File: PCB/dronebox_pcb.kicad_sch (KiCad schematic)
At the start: 17 parts, among them J101 Conn_02x05_Odd_Even, J102 Barrel_Jack_Switch, J103 Conn_01x02_Female, J104 Conn_01x02_Female, U101 LM386

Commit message: assign fps
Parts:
- C101, C102: footprint (none) -> Capacitor_THT:CP_Radial_D6.3mm_P2.50mm
- C103: footprint (none) -> Capacitor_THT:C_Disc_D4.7mm_W2.5mm_P5.00mm
- J101: footprint (none) -> Connector_IDC:IDC-Header_2x05_P2.54mm_Vertical
- J102: footprint (none) -> Connector_BarrelJack:BarrelJack_GCT_DCJ200-10-A_Horizontal
- J103, J104: footprint (none) -> Connector_PinHeader_2.54mm:PinHeader_1x02_P2.54mm_Vertical
- R101, R102, R103, R104, R105: footprint (none) -> Resistor_THT:R_Axial_DIN0207_L6.3mm_D2.5mm_P2.54mm_Vertical
- U101: footprint (none) -> Package_DIP:DIP-8_W7.62mm_Socket_LongPads
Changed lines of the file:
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@@
       (effects (font (size 1.27 1.27)) (justify left))
     )
-    (property "Footprint" "" (id 2) (at 87.122 170.18 90)
+    (property "Footprint" "Resistor_THT:R_Axial_DIN0207_L6.3mm_D2.5mm_P2.54mm_Vertical" (id 2) (at 87.122 170.18 90)
       (effects (font (size 1.27 1.27)) hide)
     )
@@
     (property "Reference" "R102" (id 0) (at 109.22 170.18 90))
     (property "Value" "10K" (id 1) (at 109.22 172.72 90))
-    (property "Footprint" "" (id 2) (at 109.22 178.308 90)
+    (property "Footprint" "Resistor_THT:R_Axial_DIN0207_L6.3mm_D2.5mm_P2.54mm_Vertical" (id 2) (at 109.22 178.308 90)
       (effects (font (size 1.27 1.27)) hide)
     )
@@
     (property "Reference" "R103" (id 0) (at 185.42 168.91 90))
     (property "Value" "10M" (id 1) (at 185.42 171.45 90))
-    (property "Footprint" "" (id 2) (at 185.42 177.038 90)
+    (property "Footprint" "Resistor_THT:R_Axial_DIN0207_L6.3mm_D2.5mm_P2.54mm_Vertical" (id 2) (at 185.42 177.038 90)
       (effects (font (size 1.27 1.27)) hide)
     )
@@
     (property "Reference" "R104" (id 0) (at 186.69 158.75 90))
     (property "Value" "680K" (id 1) (at 186.69 161.29 90))
-    (property "Footprint" "" (id 2) (at 186.69 166.878 90)
+    (property "Footprint" "Resistor_THT:R_Axial_DIN0207_L6.3mm_D2.5mm_P2.54mm_Vertical" (id 2) (at 186.69 166.878 90)
       (effects (font (size 1.27 1.27)) hide)
     )
@@
     (property "Reference" "R105" (id 0) (at 210.82 158.75 90))
     (property "Value" "100K" (id 1) (at 210.82 161.29 90))
-    (property "Footprint" "" (id 2) (at 210.82 166.878 90)
+    (property "Footprint" "Resistor_THT:R_Axial_DIN0207_L6.3mm_D2.5mm_P2.54mm_Vertical" (id 2) (at 210.82 166.878 90)
       (effects (font (size 1.27 1.27)) hide)
     )
@@
       (effects (font (size 1.27 1.27)) (justify left))
     )
-    (property "Footprint" "" (id 2) (at 124.46 184.15 0)
+    (property "Footprint" "Connector_PinHeader_2.54mm:PinHeader_1x02_P2.54mm_Vertical" (id 2) (at 124.46 184.15 0)
       (effects (font (size 1.27 1.27)) hide)
     )
@@
     (property "Reference" "J104" (id 0) (at 159.9057 167.64 0))
     (property "Value" "Conn_01x02_Female" (id 1) (at 157.3657 172.72 0))
-    (property "Footprint" "" (id 2) (at 163.83 168.91 0)
+    (property "Footprint" "Connector_PinHeader_2.54mm:PinHeader_1x02_P2.54mm_Vertical" (id 2) (at 163.83 168.91 0)
       (effects (font (size 1.27 1.27)) hide)
     )
@@
       (effects (font (size 1.27 1.27)) (justify left))
     )
-    (property "Footprint" "" (id 2) (at 101.2952 191.77 0)
+    (property "Footprint" "Capacitor_THT:CP_Radial_D6.3mm_P2.50mm" (id 2) (at 101.2952 191.77 0)
       (effects (font (size 1.27 1.27)) hide)
     )
@@
       (effects (font (size 1.27 1.27)) (justify left))
     )
-    (property "Footprint" "" (id 2) (at 120.3452 184.15 0)
+    (property "Footprint" "Capacitor_THT:CP_Radial_D6.3mm_P2.50mm" (id 2) (at 120.3452 184.15 0)
       (effects (font (size 1.27 1.27)) hide)
     )
@@
     (property "Reference" "C103" (id 0) (at 138.43 168.91 90))
     (property "Value" "C" (id 1) (at 138.43 171.45 90))
-    (property "Footprint" "" (id 2) (at 142.24 175.5648 0)
+    (property "Footprint" "Capacitor_THT:C_Disc_D4.7mm_W2.5mm_P5.00mm" (id 2) (at 142.24 175.5648 0)
       (effects (font (size 1.27 1.27)) hide)
     )
@@
     (property "Reference" "J102" (id 0) (at 40.5765 184.15 0))
     (property "Value" "Barrel_Jack_Switch" (id 1) (at 40.5765 186.69 0))
-    (property "Footprint" "" (id 2) (at 40.64 194.056 0)
+    (property "Footprint" "Connector_BarrelJack:BarrelJack_GCT_DCJ200-10-A_Horizontal" (id 2) (at 40.64 194.056 0)
       (effects (font (size 1.27 1.27)) hide)
     )
@@
     (property "Reference" "J101" (id 0) (at 40.64 165.1 0))
     (property "Value" "Conn_02x05_Odd_Even" (id 1) (at 40.64 167.64 0))
-    (property "Footprint" "" (id 2) (at 39.37 176.53 0)
+    (property "Footprint" "Connector_IDC:IDC-Header_2x05_P2.54mm_Vertical" (id 2) (at 39.37 176.53 0)
       (effects (font (size 1.27 1.27)) hide)
     )
@@
       (effects (font (size 1.27 1.27)) (justify left))
     )
-    (property "Footprint" "" (id 2) (at 100.33 173.99 0)
+    (property "Footprint" "Package_DIP:DIP-8_W7.62mm_Socket_LongPads" (id 2) (at 100.33 173.99 0)
       (effects (font (size 1.27 1.27)) hide)
     )
@@
     )
     (path "/5240ec53-33b9-435c-b4ec-4b26d289327a"
-      (reference "C101") (unit 1) (value "C_Polarized") (footprint "")
+      (reference "C101") (unit 1) (value "C_Polarized") (footprint "Capacitor_THT:CP_Radial_D6.3mm_P2.50mm")
     )
     (path "/f441d27f-51ef-4c03-be33-04c25f558c99"
-      (reference "C102") (unit 1) (value "C_Polarized") (footprint "")
+      (reference "C102") (unit 1) (value "C_Polarized") (footprint "Capacitor_THT:CP_Radial_D6.3mm_P2.50mm")
     )
     (path "/87153b71-5d6b-4536-9f6c-e8a6d609b08d"
-      (reference "C103") (unit 1) (value "C") (footprint "")
+      (reference "C103") (unit 1) (value "C") (footprint "Capacitor_THT:C_Disc_D4.7mm_W2.5mm_P5.00mm")
     )
     (path "/fc76fb76-ac0b-49bd-acbc-9d9595441908/6a12e8f9-f679-4602-8c7e-9d7159b8f50a"
@@
     )
     (path "/dfd771ef-ec0d-4a98-968b-fdbc253d052f"
-      (reference "J101") (unit 1) (value "Conn_02x05_Odd_Even") (footprint "")
+      (reference "J101") (unit 1) (value "Conn_02x05_Odd_Even") (footprint "Connector_IDC:IDC-Header_2x05_P2.54mm_Vertical")
     )
     (path "/44f20cf3-1d50-4bdd-bb81-67a45e4dcbe7"
-      (reference "J102") (unit 1) (value "Barrel_Jack_Switch") (footprint "")
+      (reference "J102") (unit 1) (value "Barrel_Jack_Switch") (footprint "Connector_BarrelJack:BarrelJack_GCT_DCJ200-10-A_Horizontal")
     )
     (path "/1a3afbf2-3f76-40d5-9865-566375212075"
-      (reference "J103") (unit 1) (value "Conn_01x02_Female") (footprint "")
+      (reference "J103") (unit 1) (value "Conn_01x02_Female") (footprint "Connector_PinHeader_2.54mm:PinHeader_1x02_P2.54mm_Vertical")
     )
     (path "/6dc13e0b-83ee-439e-b9a6-dfa782366ecd"
-      (reference "J104") (unit 1) (value "Conn_01x02_Female") (footprint "")
+      (reference "J104") (unit 1) (value "Conn_01x02_Female") (footprint "Connector_PinHeader_2.54mm:PinHeader_1x02_P2.54mm_Vertical")
     )
     (path "/fc76fb76-ac0b-49bd-acbc-9d9595441908/9a2ca155-c663-4ac0-ad7e-5c240eff215f"
@@
     )
     (path "/4a0758f4-01e2-4b91-8e0c-d7561b5cf65e"
-      (reference "R101") (unit 1) (value "4K7") (footprint "")
+      (reference "R101") (unit 1) (value "4K7") (footprint "Resistor_THT:R_Axial_DIN0207_L6.3mm_D2.5mm_P2.54mm_Vertical")
     )
     (path "/62db6c45-8a95-4b2c-8549-f31c65d548eb"
-      (reference "R102") (unit 1) (value "10K") (footprint "")
+      (reference "R102") (unit 1) (value "10K") (footprint "Resistor_THT:R_Axial_DIN0207_L6.3mm_D2.5mm_P2.54mm_Vertical")
     )
     (path "/e86b1d0f-b9ac-4267-af6a-4cf93222bdc3"
-      (reference "R103") (unit 1) (value "10M") (footprint "")
+      (reference "R103") (unit 1) (value "10M") (footprint "Resistor_THT:R_Axial_DIN0207_L6.3mm_D2.5mm_P2.54mm_Vertical")
     )
     (path "/35c58f7c-a887-45ec-8b61-a015f0c1a6b1"
-      (reference "R104") (unit 1) (value "680K") (footprint "")
+      (reference "R104") (unit 1) (value "680K") (footprint "Resistor_THT:R_Axial_DIN0207_L6.3mm_D2.5mm_P2.54mm_Vertical")
     )
     (path "/c2124b99-19a6-4951-b19a-d6bea33e316b"
-      (reference "R105") (unit 1) (value "100K") (footprint "")
+      (reference "R105") (unit 1) (value "100K") (footprint "Resistor_THT:R_Axial_DIN0207_L6.3mm_D2.5mm_P2.54mm_Vertical")
     )
     (path "/fc76fb76-ac0b-49bd-acbc-9d9595441908/6fdc68b6-2980-4a3e-894b-7f4781b4b9c0"
@@
     )
     (path "/81154892-4749-4fc6-9b00-f761a510f30f"
-      (reference "U101") (unit 1) (value "LM386") (footprint "")
+      (reference "U101") (unit 1) (value "LM386") (footprint "Package_DIP:DIP-8_W7.62mm_Socket_LongPads")
     )
   )

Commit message: rough prices
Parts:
- C101, C102, J101, J102: Price (none) -> 0.05
- C103: Price (none) -> 0.02
- R101, R102, R103, R104, R105: Price (none) -> 0.015
- RV101, RV102, RV103, RV104: Price (none) -> 0.06
- U101: Price (none) -> 0.23
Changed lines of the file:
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@@
+      (effects (font (size 1.27 1.27)) hide)
+    )
+    (property "Price" "0.015" (id 4) (at 88.9 170.18 0)
       (effects (font (size 1.27 1.27)) hide)
     )
@@
       (effects (font (size 1.27 1.27)) hide)
     )
+    (property "Price" "0.015" (id 4) (at 109.22 176.53 0)
+      (effects (font (size 1.27 1.27)) hide)
+    )
     (pin "1")
     (pin "2")
@@
       (effects (font (size 1.27 1.27)) hide)
     )
+    (property "Price" "0.015" (id 4) (at 185.42 175.26 0)
+      (effects (font (size 1.27 1.27)) hide)
+    )
     (pin "1")
     (pin "2")
@@
       (effects (font (size 1.27 1.27)) hide)
     )
+    (property "Price" "0.015" (id 4) (at 186.69 165.1 0)
+      (effects (font (size 1.27 1.27)) hide)
+    )
     (pin "1")
     (pin "2")
@@
       (effects (font (size 1.27 1.27)) hide)
     )
+    (property "Price" "0.015" (id 4) (at 210.82 165.1 0)
+      (effects (font (size 1.27 1.27)) hide)
+    )
     (pin "1")
     (pin "2")
@@
       (effects (font (size 1.27 1.27)) hide)
     )
+    (property "Price" "0.05" (id 4) (at 100.33 187.96 0)
+      (effects (font (size 1.27 1.27)) hide)
+    )
     (pin "1")
     (pin "2")
@@
     )
     (property "Datasheet" "~" (id 3) (at 119.38 180.34 0)
+      (effects (font (size 1.27 1.27)) hide)
+    )
+    (property "Price" "0.05" (id 4) (at 119.38 180.34 0)
       (effects (font (size 1.27 1.27)) hide)
     )
@@
       (effects (font (size 1.27 1.27)) hide)
     )
+    (property "Price" "0.02" (id 4) (at 138.43 176.53 0)
+      (effects (font (size 1.27 1.27)) hide)
+    )
     (pin "1")
     (pin "2")
@@
       (effects (font (size 1.27 1.27)) hide)
     )
+    (property "Price" "0.06" (id 4) (at 130.81 176.53 0)
+      (effects (font (size 1.27 1.27)) hide)
+    )
     (pin "1")
     (pin "2")
@@
       (effects (font (size 1.27 1.27)) hide)
     )
+    (property "Price" "0.06" (id 4) (at 172.72 168.91 0)
+      (effects (font (size 1.27 1.27)) hide)
+    )
     (pin "1")
     (pin "2")
@@
       (effects (font (size 1.27 1.27)) hide)
     )
+    (property "Price" "0.06" (id 4) (at 199.39 165.1 0)
+      (effects (font (size 1.27 1.27)) hide)
+    )
     (pin "1")
     (pin "2")
@@
       (effects (font (size 1.27 1.27)) hide)
     )
+    (property "Price" "0.06" (id 4) (at 218.44 165.1 0)
+      (effects (font (size 1.27 1.27)) hide)
+    )
     (pin "1")
     (pin "2")
@@
       (effects (font (size 1.27 1.27)) hide)
     )
+    (property "Price" "0.05" (id 4) (at 39.37 193.04 0)
+      (effects (font (size 1.27 1.27)) hide)
+    )
     (pin "1")
     (pin "2")
@@
     )
     (property "Datasheet" "~" (id 3) (at 39.37 176.53 0)
+      (effects (font (size 1.27 1.27)) hide)
+    )
+    (property "Price" "0.05" (id 4) (at 39.37 176.53 0)
       (effects (font (size 1.27 1.27)) hide)
     )
@@
       (effects (font (size 1.27 1.27)) hide)
     )
+    (property "Price" "0.23" (id 4) (at 97.79 176.53 0)
+      (effects (font (size 1.27 1.27)) hide)
+    )

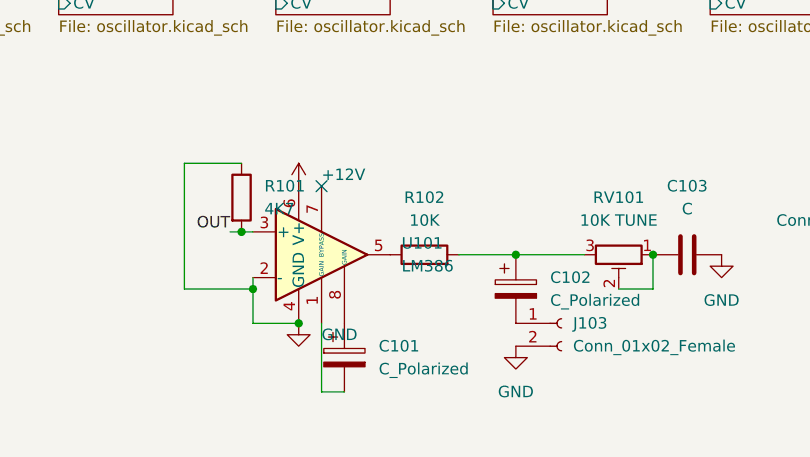
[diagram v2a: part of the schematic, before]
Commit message: update to smd components
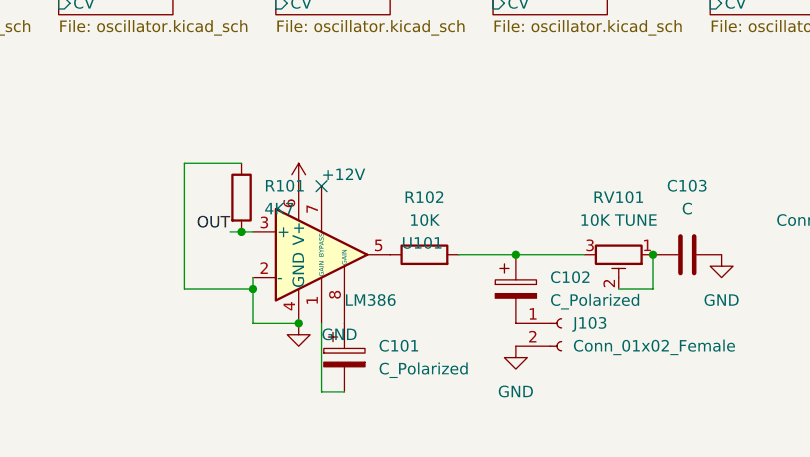
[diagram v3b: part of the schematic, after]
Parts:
- R101, R102, R103, R104, R105: footprint Resistor_THT:R_Axial_DIN0207_L6.3mm_D2.5mm_P2.54mm_Vertical -> Resistor_SMD:R_1206_3216Metric_Pad1.30x1.75mm_HandSolder
